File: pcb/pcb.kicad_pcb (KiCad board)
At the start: 2 copper layers, 40.6 x 50.8 mm, 7 parts, among them SW1 SW_Push, U1 NodeMCU1.0(ESP-12E), U2 DHT22, U3 SSD1306_OLED_128x32, U4 VL6180X_Adafruit

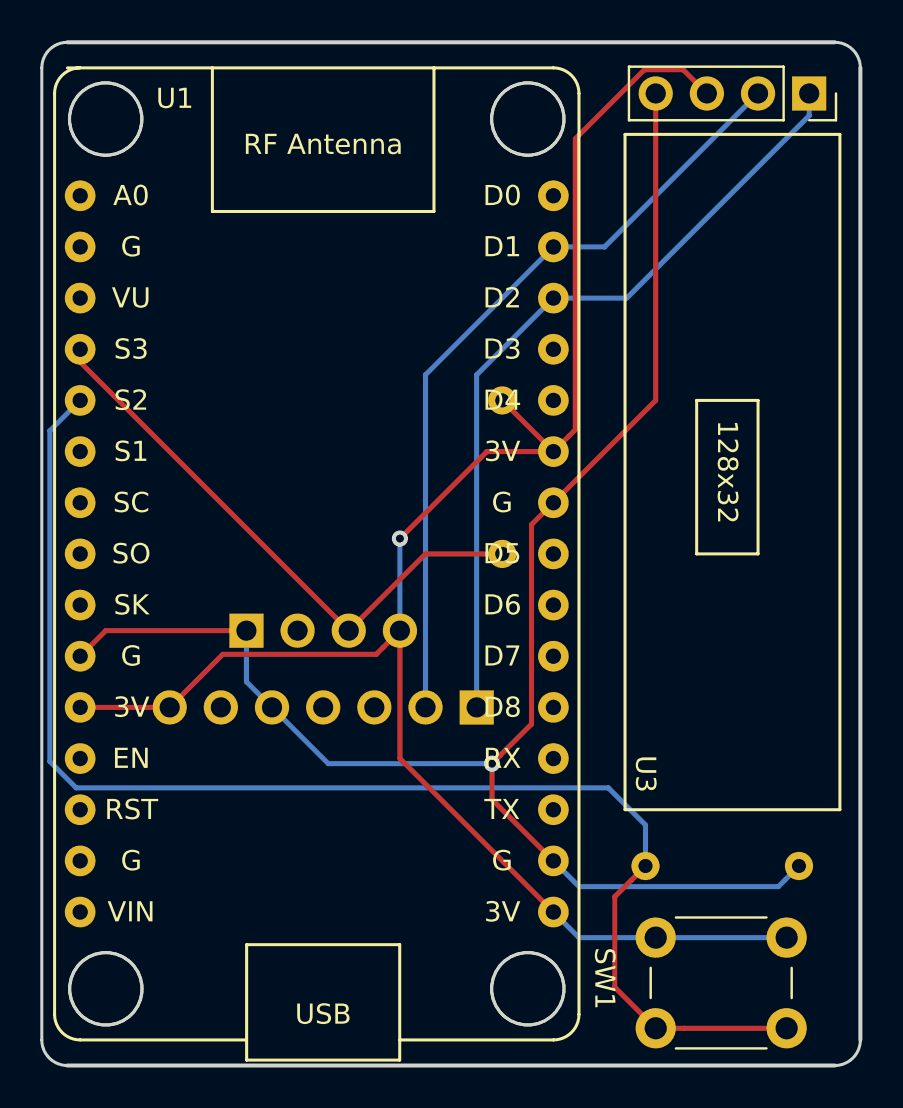
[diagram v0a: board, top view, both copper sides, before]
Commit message: Add ground plane
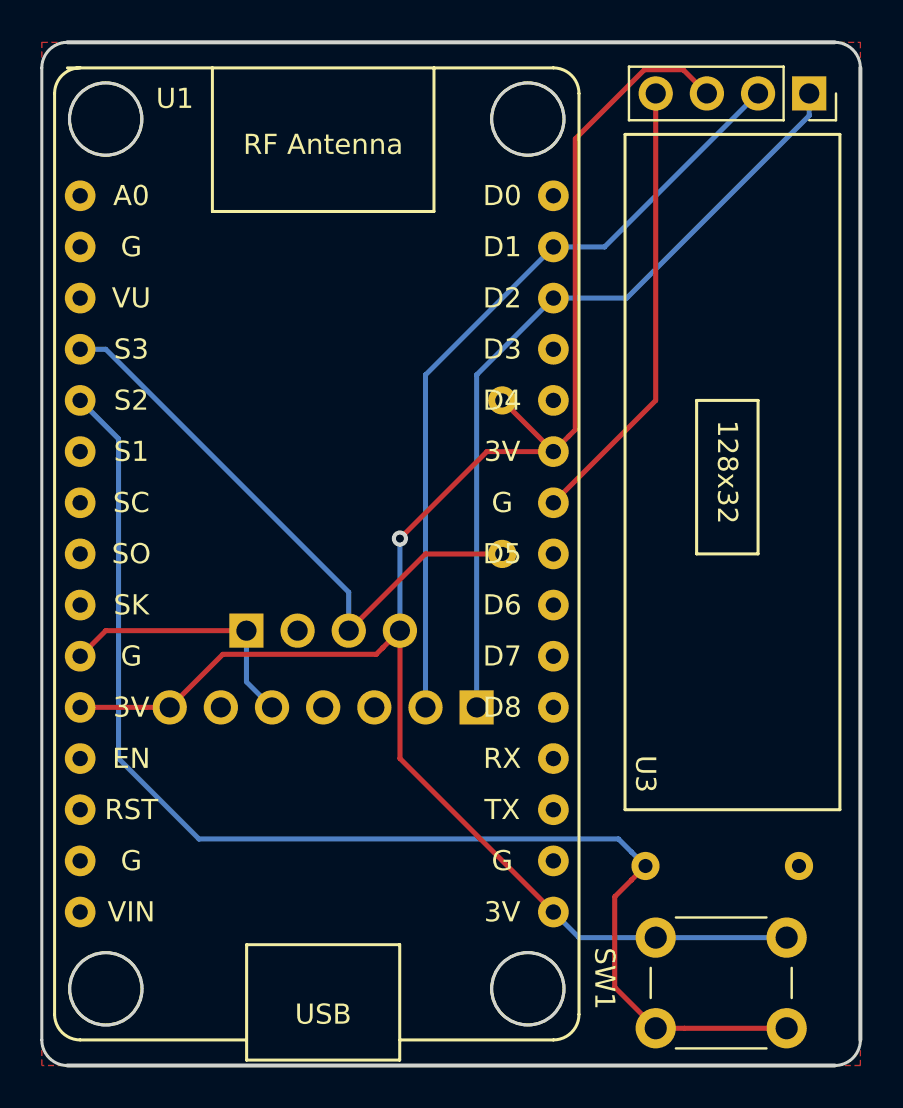
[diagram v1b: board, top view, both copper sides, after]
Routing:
- net GND: track 81.1 -> 35.5 mm, vias 1 -> 0
- net Net-(R2-Pad1): track 67.5 -> 63.0 mm
- net Net-(R1-Pad2): track 28.7 -> 29.4 mm
- added copper zone on F.Cu, net GND
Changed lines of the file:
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@@
     (thickness 1.6)
     (drawings 17)
-    (tracks 67)
+    (tracks 55)
     (zones 0)
     (modules 7)
@@
   (segment (start 167.64 119.38) (end 163.83 119.38) (width 0.25) (layer B.Cu) (net 24))
   (segment (start 174.14 119.38) (end 167.64 119.38) (width 0.25) (layer B.Cu) (net 24))
-  (segment (start 147.32 106.68) (end 148.59 107.95) (width 0.25) (layer B.Cu) (net 25))
-  (segment (start 147.32 104.14) (end 147.32 106.68) (width 0.25) (layer B.Cu) (net 25))
   (segment (start 140.335 104.14) (end 139.065 105.41) (width 0.25) (layer F.Cu) (net 25))
   (segment (start 147.32 104.14) (end 140.335 104.14) (width 0.25) (layer F.Cu) (net 25))
   (segment (start 167.64 92.71) (end 162.56 97.79) (width 0.25) (layer F.Cu) (net 25))
   (segment (start 167.64 77.47) (end 167.64 92.71) (width 0.25) (layer F.Cu) (net 25))
-  (via (at 159.512 110.744) (size 0.8) (drill 0.4) (layers F.Cu B.Cu) (net 25))
-  (segment (start 148.59 107.95) (end 151.384 110.744) (width 0.25) (layer B.Cu) (net 25))
-  (segment (start 151.384 110.744) (end 159.512 110.744) (width 0.25) (layer B.Cu) (net 25))
-  (segment (start 159.512 112.522) (end 162.56 115.57) (width 0.25) (layer F.Cu) (net 25))
-  (segment (start 159.512 110.744) (end 159.512 112.522) (width 0.25) (layer F.Cu) (net 25))
-  (segment (start 159.911999 110.344001) (end 159.512 110.744) (width 0.25) (layer F.Cu) (net 25))
-  (segment (start 161.472999 108.783001) (end 159.911999 110.344001) (width 0.25) (layer F.Cu) (net 25))
-  (segment (start 161.472999 98.877001) (end 161.472999 108.783001) (width 0.25) (layer F.Cu) (net 25))
-  (segment (start 162.56 97.79) (end 161.472999 98.877001) (width 0.25) (layer F.Cu) (net 25))
-  (segment (start 174.052001 116.523999) (end 174.752 115.824) (width 0.25) (layer B.Cu) (net 25))
-  (segment (start 173.726999 116.849001) (end 174.052001 116.523999) (width 0.25) (layer B.Cu) (net 25))
-  (segment (start 163.839001 116.849001) (end 173.726999 116.849001) (width 0.25) (layer B.Cu) (net 25))
-  (segment (start 162.56 115.57) (end 163.839001 116.849001) (width 0.25) (layer B.Cu) (net 25))
+  (segment (start 147.32 106.68) (end 148.59 107.95) (width 0.25) (layer B.Cu) (net 25))
+  (segment (start 147.32 104.14) (end 147.32 106.68) (width 0.25) (layer B.Cu) (net 25))
   (segment (start 156.21 100.33) (end 160.02 100.33) (width 0.25) (layer F.Cu) (net 26))
   (segment (start 152.4 104.14) (end 156.21 100.33) (width 0.25) (layer F.Cu) (net 26))
-  (segment (start 139.065 90.805) (end 139.065 90.17) (width 0.25) (layer F.Cu) (net 26))
-  (segment (start 152.4 104.14) (end 139.065 90.805) (width 0.25) (layer F.Cu) (net 26))
-  (segment (start 165.282999 111.942999) (end 167.132 113.792) (width 0.25) (layer B.Cu) (net 30))
-  (segment (start 167.132 113.792) (end 167.132 115.824) (width 0.25) (layer B.Cu) (net 30))
-  (segment (start 139.065 92.71) (end 137.56001 94.21499) (width 0.25) (layer B.Cu) (net 30))
-  (segment (start 138.866999 111.942999) (end 165.282999 111.942999) (width 0.25) (layer B.Cu) (net 30))
-  (segment (start 137.56001 110.63601) (end 138.866999 111.942999) (width 0.25) (layer B.Cu) (net 30))
-  (segment (start 137.56001 94.21499) (end 137.56001 110.63601) (width 0.25) (layer B.Cu) (net 30))
+  (segment (start 152.4 104.14) (end 152.4 102.235) (width 0.25) (layer B.Cu) (net 26))
+  (segment (start 140.335 90.17) (end 139.065 90.17) (width 0.25) (layer B.Cu) (net 26))
+  (segment (start 152.4 102.235) (end 140.335 90.17) (width 0.25) (layer B.Cu) (net 26))
   (segment (start 166.432001 116.523999) (end 167.132 115.824) (width 0.25) (layer F.Cu) (net 30))
   (segment (start 165.608 117.348) (end 166.432001 116.523999) (width 0.25) (layer F.Cu) (net 30))
@@
   (segment (start 169.054213 123.88) (end 174.14 123.88) (width 0.25) (layer F.Cu) (net 30))
   (segment (start 167.64 123.88) (end 169.054213 123.88) (width 0.25) (layer F.Cu) (net 30))
+  (segment (start 166.432001 115.124001) (end 167.132 115.824) (width 0.25) (layer B.Cu) (net 30))
+  (segment (start 165.790999 114.482999) (end 166.432001 115.124001) (width 0.25) (layer B.Cu) (net 30))
+  (segment (start 144.962999 114.482999) (end 165.790999 114.482999) (width 0.25) (layer B.Cu) (net 30))
+  (segment (start 140.97 110.49) (end 144.962999 114.482999) (width 0.25) (layer B.Cu) (net 30))
+  (segment (start 139.065 92.71) (end 140.97 94.615) (width 0.25) (layer B.Cu) (net 30))
+  (segment (start 140.97 94.615) (end 140.97 110.49) (width 0.25) (layer B.Cu) (net 30))
+  (zone (net 25) (net_name GND) (layer F.Cu) (hatch edge 0.508)
+    (connect_pads (clearance 0.508))
+    (min_thickness 0.254)
+    (fill yes (arc_segments 16) (thermal_gap 0.508) (thermal_bridge_width 0.508))
+    (polygon
+      (pts
+        (xy 137.16 74.93) (xy 177.8 74.93) (xy 177.8 125.73) (xy 137.16 125.73)
+      )
+    )
+  )
 )

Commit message: Minor changes before gerber export
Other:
- board text added: "Levain Monitor V1.0 J.Lam - 2020/05/13"
- board text removed: "JLAM V1.0 2020-05-12"
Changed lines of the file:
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@@
   (page A4)
   (layers
-    (0 F.Cu signal hide)
+    (0 F.Cu signal)
     (31 B.Cu signal)
-    (32 B.Adhes user hide)
-    (33 F.Adhes user hide)
+    (32 B.Adhes user)
+    (33 F.Adhes user)
     (34 B.Paste user)
-    (35 F.Paste user hide)
+    (35 F.Paste user)
     (36 B.SilkS user)
-    (37 F.SilkS user hide)
+    (37 F.SilkS user)
     (38 B.Mask user)
-    (39 F.Mask user hide)
-    (40 Dwgs.User user hide)
-    (41 Cmts.User user hide)
-    (42 Eco1.User user hide)
-    (43 Eco2.User user hide)
+    (39 F.Mask user)
+    (40 Dwgs.User user)
+    (41 Cmts.User user)
+    (42 Eco1.User user)
+    (43 Eco2.User user)
     (44 Edge.Cuts user)
-    (45 Margin user hide)
+    (45 Margin user)
     (46 B.CrtYd user)
-    (47 F.CrtYd user hide)
+    (47 F.CrtYd user)
     (48 B.Fab user)
-    (49 F.Fab user hide)
+    (49 F.Fab user)
   )
   (setup
@@
       (effects (font (size 1 1) (thickness 0.15)))
     )
-    (fp_text value SSD1306_OLED_128x32 (at 0 10.39 270) (layer F.Fab)
+    (fp_text value SSD1306_OLED_128x32 (at 11.43 8.128 270 unlocked) (layer F.Fab)
       (effects (font (size 1 1) (thickness 0.15)))
     )
@@
     (descr https://www.omron.com/ecb/products/pdf/en-b3f.pdf)
     (tags "tact sw push 6mm")
-    (fp_text reference SW1 (at -2.54 2.032 -90 unlocked) (layer F.SilkS)
+    (fp_text reference SW1 (at -1.778 2.159 -90 unlocked) (layer F.SilkS)
       (effects (font (size 1 1) (thickness 0.15)))
     )
@@
     )
   )
-  (gr_circle (center 140.346051 78.74) (end 142.15106 78.74) (layer B.Mask) (width 1))
-  (gr_circle (center 140.346051 121.92) (end 142.15106 121.92) (layer B.Mask) (width 1))
-  (gr_circle (center 161.29 121.92) (end 163.095009 121.92) (layer B.Mask) (width 1))
-  (gr_circle (center 161.29 78.74) (end 163.095009 78.74) (layer B.Mask) (width 1))
+  (gr_circle (center 140.346051 78.74) (end 142.15106 78.74) (layer B.Mask) (width 2))
+  (gr_circle (center 140.346051 121.92) (end 142.15106 121.92) (layer B.Mask) (width 2))
+  (gr_circle (center 161.29 121.92) (end 163.095009 121.92) (layer B.Mask) (width 2))
+  (gr_circle (center 161.29 78.74) (end 163.095009 78.74) (layer B.Mask) (width 2))
   (gr_line (start 137.16 76.2) (end 137.16 124.46) (layer Edge.Cuts) (width 0.15))
   (gr_arc (start 138.43 76.2) (end 138.43 74.93) (angle -90) (layer Edge.Cuts) (width 0.15))
@@
   (gr_circle (center 161.29 78.74) (end 162.56 77.47) (layer Edge.Cuts) (width 0.15))
   (gr_circle (center 161.29 121.92) (end 162.56 120.65) (layer Edge.Cuts) (width 0.15))
-  (gr_text "JLAM   V1.0\n2020-05-12" (at 173.99 98.552 270) (layer B.SilkS)
-    (effects (font (size 1.5 1.5) (thickness 0.3)) (justify mirror))
+  (gr_text "Levain Monitor V1.0\nJ.Lam - 2020/05/13" (at 174.371 97.663 270) (layer B.SilkS)
+    (effects (font (size 1.2 1.2) (thickness 0.2)) (justify mirror))
   )
   (gr_arc (start 176.53 124.46) (end 176.53 125.73) (angle -90) (layer Edge.Cuts) (width 0.15))
